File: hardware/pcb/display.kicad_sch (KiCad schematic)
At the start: 3 parts, among them J301 DSI FPC 22P 0.5mm, J302 LCD 5V (5V/5V/GND)

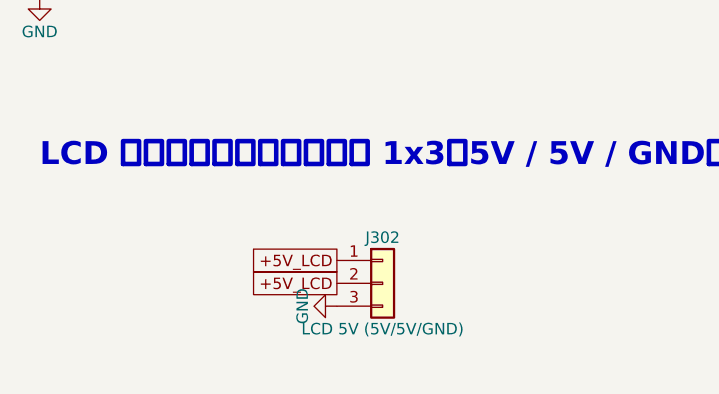
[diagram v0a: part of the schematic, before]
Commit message: Wire the power sheet and use power symbols for +5V_LCD
Replace the labels on the power sheet with wires, use power symbols for
+5V_LCD and the VBUS test pads, and change J302 to Conn_01x03_Pin.

Co-Authored-By: Claude Opus 5.5 <noreply@anthropic.com>
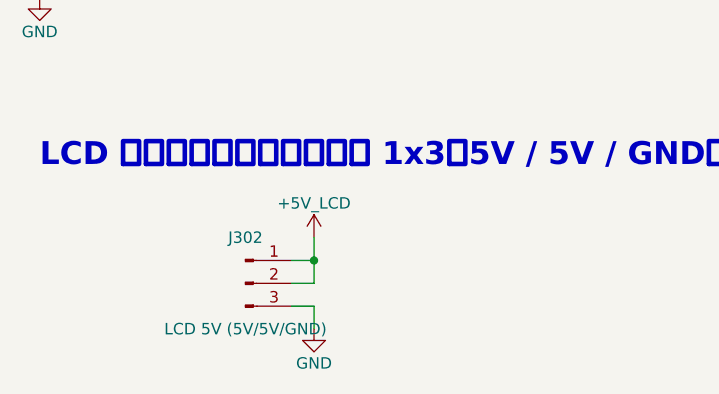
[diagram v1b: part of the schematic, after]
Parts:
- J302: symbol Connector_Generic:Conn_01x03 -> Connector:Conn_01x03_Pin
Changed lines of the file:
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@@
 		)
+	)
+	(junction
+		(at 170.18 187.96)
+		(diameter 0)
+		(color 0 0 0 0)
 	)
 	(no_connect
@@
 	(no_connect
 		(at 172.72 119.38)
+	)
+	(wire
+		(pts
+			(xy 170.18 193.04) (xy 170.18 195.58)
+		)
+		(stroke
+			(width 0)
+			(type default)
+		)
+	)
+	(wire
+		(pts
+			(xy 170.18 187.96) (xy 170.18 185.42)
+		)
+		(stroke
+			(width 0)
+			(type default)
+		)
+	)
+	(wire
+		(pts
+			(xy 167.64 190.5) (xy 170.18 190.5)
+		)
+		(stroke
+			(width 0)
+			(type default)
+		)
+	)
+	(wire
+		(pts
+			(xy 167.64 187.96) (xy 170.18 187.96)
+		)
+		(stroke
+			(width 0)
+			(type default)
+		)
+	)
+	(wire
+		(pts
+			(xy 170.18 190.5) (xy 170.18 187.96)
+		)
+		(stroke
+			(width 0)
+			(type default)
+		)
+	)
+	(wire
+		(pts
+			(xy 167.64 193.04) (xy 170.18 193.04)
+		)
+		(stroke
+			(width 0)
+			(type default)
+		)
 	)
 	(global_label "DSI_D0_N"
@@
 		)
 	)
-	(global_label "+5V_LCD"
-		(shape passive)
-		(at 172.72 187.96 180)
-		(fields_autoplaced yes)
-		(effects
-			(font
-				(size 1.27 1.27)
-			)
-			(justify right)
-		)
-		(property "Intersheetrefs" "${INTERSHEET_REFS}"
-			(at 172.72 187.96 0)
-			(hide yes)
-			(show_name no)
-			(do_not_autoplace no)
-			(effects
-				(font
-					(size 1.27 1.27)
-				)
-			)
-		)
-	)
 	(global_label "DSI_D1_P"
 		(shape passive)
@@
 		(property "Intersheetrefs" "${INTERSHEET_REFS}"
 			(at 172.72 111.76 0)
-			(hide yes)
-			(show_name no)
-			(do_not_autoplace no)
-			(effects
-				(font
-					(size 1.27 1.27)
-				)
-			)
-		)
-	)
-	(global_label "+5V_LCD"
-		(shape passive)
-		(at 172.72 190.5 180)
-		(fields_autoplaced yes)
-		(effects
-			(font
-				(size 1.27 1.27)
-			)
-			(justify right)
-		)
-		(property "Intersheetrefs" "${INTERSHEET_REFS}"
-			(at 172.72 190.5 0)
 			(hide yes)
 			(show_name no)
@@
 	)
 	(symbol
+		(lib_id "power:+5V")
+		(at 170.18 185.42 0)
+		(unit 1)
+		(body_style 1)
+		(exclude_from_sim no)
+		(in_bom yes)
+		(on_board yes)
+		(in_pos_files yes)
+		(dnp no)
+		(property "Reference" "#PWR010"
+			(at 170.18 189.23 0)
+			(hide yes)
+			(show_name no)
+			(do_not_autoplace no)
+			(effects
+				(font
+					(size 1.27 1.27)
+				)
+			)
+		)
+		(property "Value" "+5V_LCD"
+			(at 170.18 181.61 0)
+			(show_name no)
+			(do_not_autoplace no)
+			(effects
+				(font
+					(size 1.27 1.27)
+				)
+			)
+		)
+		(property "Footprint" ""
+			(at 170.18 185.42 0)
+			(hide yes)
+			(show_name no)
+			(do_not_autoplace no)
+			(effects
+				(font
+					(size 1.27 1.27)
+				)
+			)
+		)
+		(property "Datasheet" ""
+			(at 170.18 185.42 0)
+			(hide yes)
+			(show_name no)
+			(do_not_autoplace no)
+			(effects
+				(font
+					(size 1.27 1.27)
+				)
+			)
+		)
+		(property "Description" "Power symbol creates a global label with name \"+5V\""
+			(at 170.18 185.42 0)
+			(hide yes)
+			(show_name no)
+			(do_not_autoplace no)
+			(effects
+				(font
+					(size 1.27 1.27)
+				)
+			)
+		)
+		(pin "1"
+		)
+		(instances
+			(project "skjar"
+				(path "/1040ccb5-ae9e-4b0f-85c7-cf44771f813b/a0d89e2a-0804-4656-835c-28eaccbeaafa"
+					(reference "#PWR010")
+					(unit 1)
+				)
+			)
+		)
+	)
+	(symbol
 		(lib_id "power:GND")
 		(at 139.7 158.75 0)
@@
 	)
 	(symbol
-		(lib_id "Connector_Generic:Conn_01x03")
-		(at 177.8 190.5 0)
+		(lib_id "Connector:Conn_01x03_Pin")
+		(at 162.56 190.5 0)
 		(unit 1)
 		(body_style 1)
@@
 		(dnp no)
 		(property "Reference" "J302"
-			(at 177.8 185.42 0)
+			(at 162.56 185.42 0)
 			(show_name no)
 			(do_not_autoplace no)
@@
 		)
 		(property "Value" "LCD 5V (5V/5V/GND)"
-			(at 177.8 195.58 0)
+			(at 162.56 195.58 0)
 			(show_name no)
 			(do_not_autoplace no)
@@
 		)
 		(property "Footprint" ""
-			(at 177.8 190.5 0)
+			(at 162.56 190.5 0)
 			(hide yes)
 			(show_name no)
@@
 		)
 		(property "Datasheet" ""
-			(at 177.8 190.5 0)
-			(hide yes)
-			(show_name no)
-			(do_not_autoplace no)
-			(effects
-				(font
-					(size 1.27 1.27)
-				)
-			)
-		)
-		(property "Description" "Generic connector, single row, 01x03, script generated (kicad-library-utils/schlib/autogen/connector/)"
-			(at 177.8 190.5 0)
+			(at 162.56 190.5 0)
+			(hide yes)
+			(show_name no)
+			(do_not_autoplace no)
+			(effects
+				(font
+					(size 1.27 1.27)
+				)
+			)
+		)
+		(property "Description" "Generic connector, single row, 01x03, script generated"
+			(at 162.56 190.5 0)
 			(hide yes)
 			(show_name no)
@@
 	(symbol
 		(lib_id "power:GND")
-		(at 172.72 193.04 270)
+		(at 170.18 195.58 0)
 		(unit 1)
 		(body_style 1)
@@
 		(dnp no)
 		(property "Reference" "#PWR115"
-			(at 172.72 193.04 0)
+			(at 170.18 195.58 0)
 			(hide yes)
 			(show_name no)
@@
 		)
 		(property "Value" "GND"
-			(at 168.91 193.04 0)
+			(at 170.18 199.39 0)
 			(show_name no)
 			(do_not_autoplace no)
@@
 		)
 		(property "Footprint" ""
-			(at 172.72 193.04 0)
+			(at 170.18 195.58 0)
 			(hide yes)
 			(show_name no)
@@
 		)
 		(property "Datasheet" ""
-			(at 172.72 193.04 0)
+			(at 170.18 195.58 0)
 			(hide yes)
 			(show_name no)
@@
 		)
 		(property "Description" ""
-			(at 172.72 193.04 0)
-			(show_name no)
-			(do_not_autoplace no)
+			(at 170.18 195.58 0)
+			(show_name no)
+			(do_not_autoplace no)

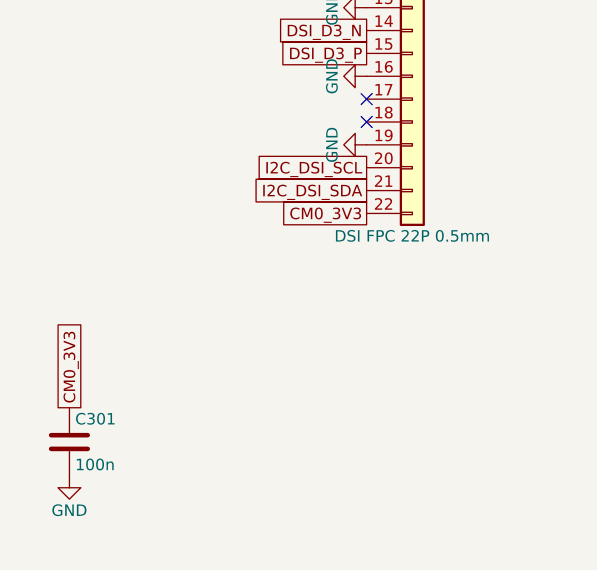
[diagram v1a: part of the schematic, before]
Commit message: Use power symbols for the CM0 3.3V and 1.8V rails
Rename CM0_3V3 to +3V3_CM0 and CM0_1V8 to +1V8_CM0, replace their
labels on the cm0, display and peripherals sheets with power symbols,
and update the docs to match.

Co-Authored-By: Claude Opus 5.5 <noreply@anthropic.com>
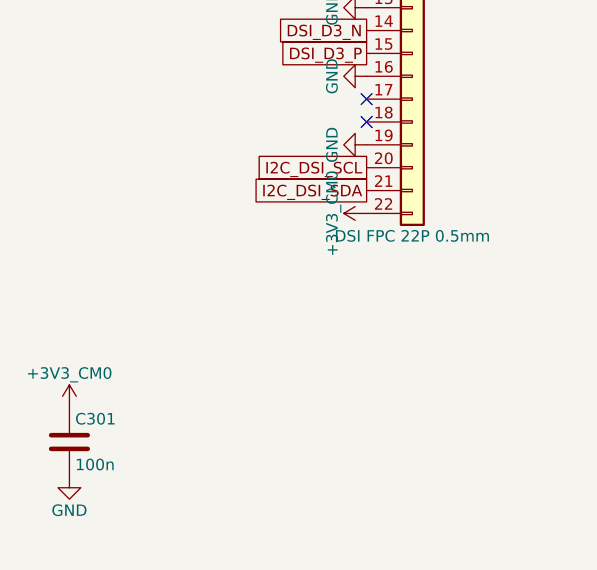
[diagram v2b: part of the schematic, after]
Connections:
- net CM0_3V3 renamed +3V3_CM0
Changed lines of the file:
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@@
-		)
-	)
-	(global_label "CM0_3V3"
-		(shape passive)
-		(at 172.72 129.54 180)
-		(fields_autoplaced yes)
-		(effects
-			(font
-				(size 1.27 1.27)
-			)
-			(justify right)
-		)
-		(property "Intersheetrefs" "${INTERSHEET_REFS}"
-			(at 172.72 129.54 0)
-			(hide yes)
-			(show_name no)
-			(do_not_autoplace no)
-			(effects
-				(font
-					(size 1.27 1.27)
-				)
-			)
 		)
 	)
@@
 		)
 	)
-	(global_label "CM0_3V3"
-		(shape passive)
-		(at 139.7 151.13 90)
-		(fields_autoplaced yes)
-		(effects
-			(font
-				(size 1.27 1.27)
-			)
-			(justify left)
-		)
-		(property "Intersheetrefs" "${INTERSHEET_REFS}"
-			(at 139.7 151.13 0)
-			(hide yes)
-			(show_name no)
-			(do_not_autoplace no)
-			(effects
-				(font
-					(size 1.27 1.27)
-				)
-			)
-		)
-	)
 	(global_label "DSI_D3_N"
 		(shape passive)
@@
 					(unit 1)
 				)
+			)
+		)
+	)
+	(symbol
+		(lib_id "power:+3V3")
+		(at 139.7 151.13 0)
+		(unit 1)
+		(exclude_from_sim no)
+		(in_bom yes)
+		(on_board yes)
+		(dnp no)
+		(property "Reference" "#PWR183"
+			(at 139.7 151.13 0)
+			(hide yes)
+			(effects
+				(font
+					(size 1.27 1.27)
+				)
+			)
+		)
+		(property "Value" "+3V3_CM0"
+			(at 139.7 147.32 0)
+			(effects
+				(font
+					(size 1.27 1.27)
+				)
+			)
+		)
+		(property "Footprint" ""
+			(at 139.7 151.13 0)
+			(hide yes)
+			(effects
+				(font
+					(size 1.27 1.27)
+				)
+			)
+		)
+		(property "Datasheet" ""
+			(at 139.7 151.13 0)
+			(hide yes)
+			(effects
+				(font
+					(size 1.27 1.27)
+				)
+			)
+		)
+		(pin "1"
+		)
+		(instances
+			(project "skjar"
+				(path "/1040ccb5-ae9e-4b0f-85c7-cf44771f813b/a0d89e2a-0804-4656-835c-28eaccbeaafa"
+					(reference "#PWR183")
+					(unit 1)
+				)
+			)
+		)
+	)
+	(symbol
+		(lib_id "power:+3V3")
+		(at 172.72 129.54 90)
+		(unit 1)
+		(exclude_from_sim no)
+		(in_bom yes)
+		(on_board yes)
+		(dnp no)
+		(property "Reference" "#PWR184"
+			(at 172.72 129.54 0)
+			(hide yes)
+			(effects
+				(font
+					(size 1.27 1.27)
+				)
+			)
+		)
+		(property "Value" "+3V3_CM0"
+			(at 168.91 129.54 0)
+			(effects
+				(font
+					(size 1.27 1.27)
+				)
+			)
+		)
+		(property "Footprint" ""
+			(at 172.72 129.54 0)
+			(hide yes)
+			(effects
+				(font
+					(size 1.27 1.27)
+				)
+			)
+		)
+		(property "Datasheet" ""
+			(at 172.72 129.54 0)
+			(hide yes)
+			(effects
+				(font
+					(size 1.27 1.27)
+				)
+			)
+		)
+		(pin "1"
+		)
+		(instances
+			(project "skjar"
+				(path "/1040ccb5-ae9e-4b0f-85c7-cf44771f813b/a0d89e2a-0804-4656-835c-28eaccbeaafa"
+					(reference "#PWR184")
+					(unit 1)
+				)

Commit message: Assign 0603 parts, use 30k for ILM, and switch the LDO to AP2127
Give every resistor and capacitor a 0603 footprint and an LCSC number
(Basic where possible), change the ILM resistor to a 30k Basic part,
and replace the XC6206 with an AP2127N-3.3 from stock. Record the
decisions and drop the resolved open items.

Co-Authored-By: Claude Opus 5.5 <noreply@anthropic.com>
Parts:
- C301: footprint (none) -> Capacitor_SMD:C_0603_1608Metric; LCSC (none) -> C14663
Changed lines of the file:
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@@
 			)
 		)
-		(property "Footprint" ""
+		(property "Footprint" "Capacitor_SMD:C_0603_1608Metric"
 			(at 140.6652 158.75 0)
 			(hide yes)
@@
 			(effects
 				(font
+					(size 1.27 1.27)
+				)
+			)
+		)
+		(property "LCSC" "C14663"
+			(at 139.7 154.94 0)
+			(show_name no)
+			(do_not_autoplace no)
+			(hide yes)
+			(effects
+				(font

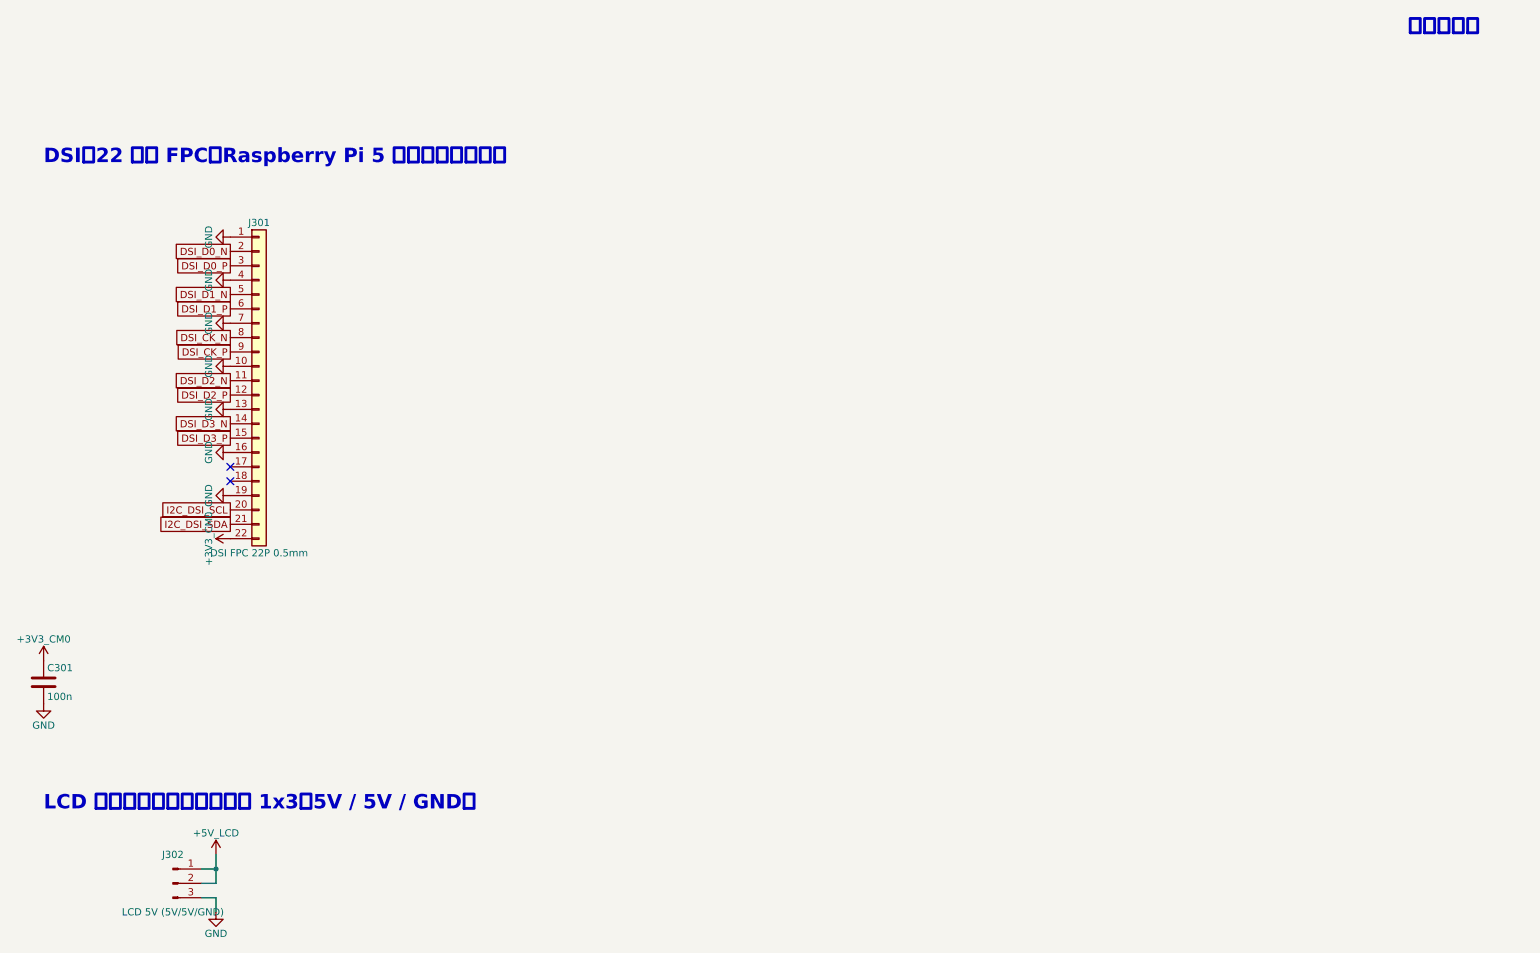
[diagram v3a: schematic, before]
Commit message: Add audio, microSD and keyboard I2C, and place parts on the PCB
Schematics:
- Swap the MAX98357A for the TLV320DAC3100 (headphone and speaker out).
  A 12 MHz oscillator drives MCLK and the codec is the I2S clock master,
  so the stock simple-audio-card works without a custom machine driver.
- Add the microSD slot for the CM0Lite; the SD pull-ups are footprints only.
- Add HID over I2C from the RP2040 to the CM0 (KB_SDA/KB_SCL/KB_INT) on
  i2c-gpio, so the keyboard works on stock Raspberry Pi OS. Add test pads.
- Use power symbols for +1V1, assign footprints and LCSC numbers, and
  fix global label shapes.

PCB: 228.6 x 146.2 mm outline and a provisional bottom-side placement,
with HID USB top-left and Linux USB top-right. Add footprints for the CM0,
TPS2121 (RUX), the 22-pin DSI FPC and the CR2032 holder.

Docs: record the decisions and open items. Add a draft device tree
overlay for the audio codec.

Co-Authored-By: Claude Opus 5.5 <noreply@anthropic.com>
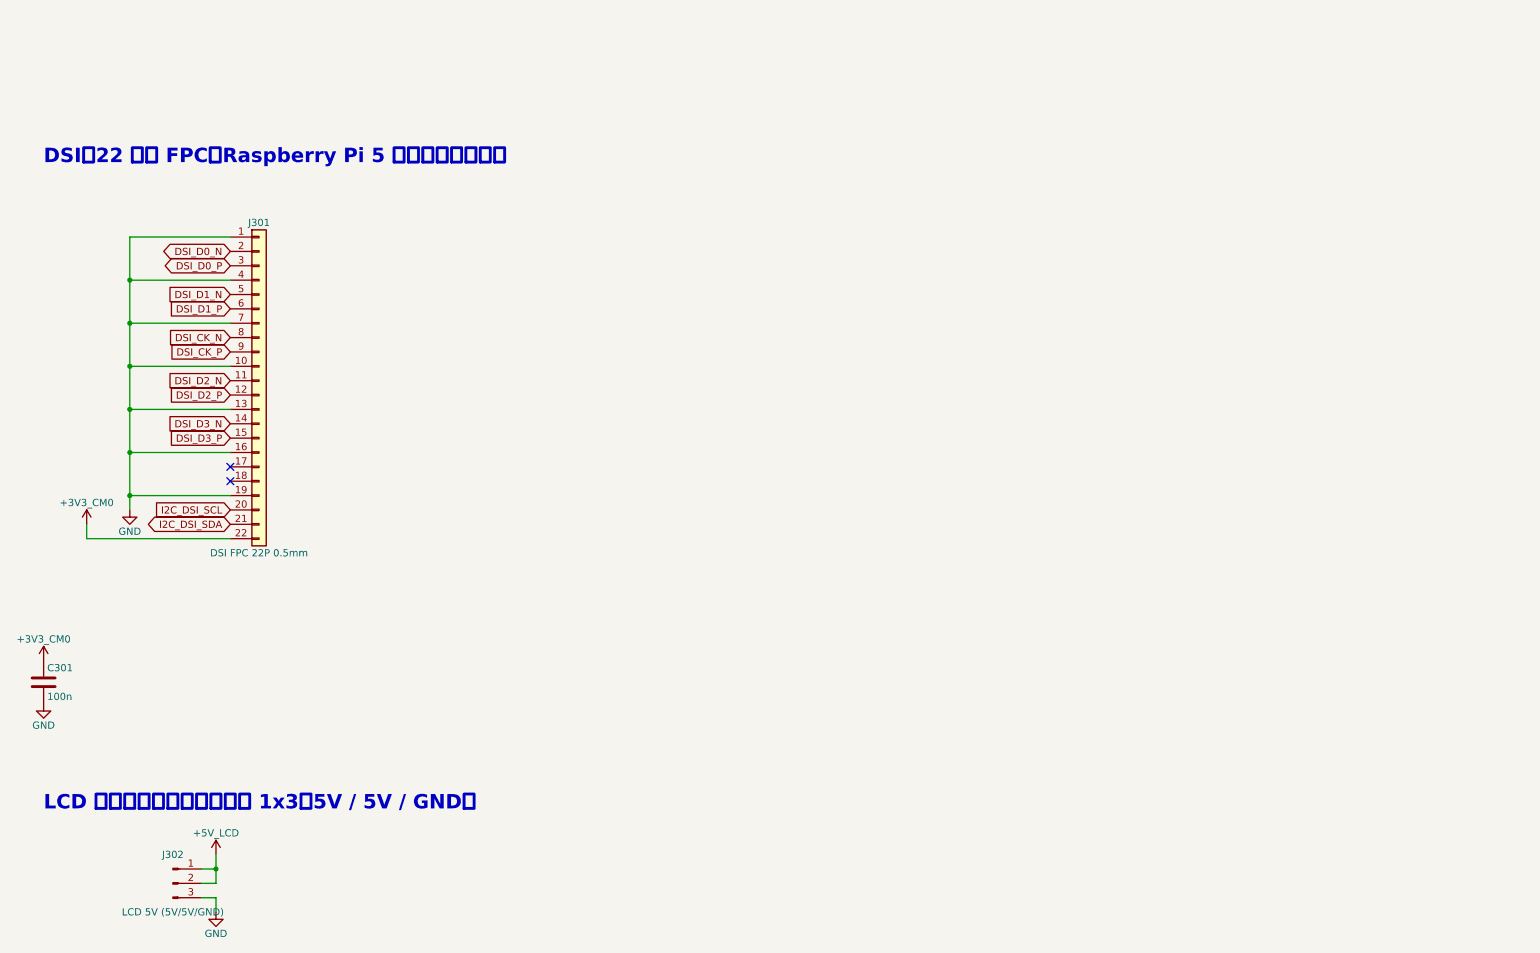
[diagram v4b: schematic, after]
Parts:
- J301: footprint (none) -> Skjar:FPC_0.5mm_22P_DualContact_HYH2.0; LCSC (none) -> C6364665
- J302: footprint (none) -> Connector_PinHeader_2.54mm:PinHeader_1x03_P2.54mm_Horizontal
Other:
- note removed: "シート外へ"
